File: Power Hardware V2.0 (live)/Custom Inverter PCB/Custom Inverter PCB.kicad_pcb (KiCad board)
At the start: 2 copper layers, 138 parts, among them J1 1714971, J2 1714971, J3 1714968, J4 SSQ-110-03-G-D, J5 SSQ-110-03-G-D, K1 1-1393210-3, K2 1-1393210-3, Q1 CSD19532Q5B, Q2 CSD19532Q5B, Q3 CSD19532Q5B, Q4 CSD19532Q5B, Q5 CSD19532Q5B, Q6 CSD19532Q5B, Q7 HCPL-181-06BE, Q8 HCPL-181-06BE, U1 DRV8300DIPWR, U2 NTR4170NT1G, U3 NTR4170NT1G, U4 TLV9004IPWR, U5 LAUNCHXL-F280049C

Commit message: footprint fixes
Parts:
- removed the C10 at (55.0, 116.9)
- removed the C10 at (104.0, 49.4)
- removed the C11 at (104.0, 52.5)
- removed the C11 at (119.0, 80.6)
- removed the C11 at (68.7, 108.3)
- removed the C12 at (108.5, 46.4)
- removed the C12 at (71.8, 108.3)
- removed the C12 at (119.0, 83.1)
- removed the C13 at (119.0, 85.6)
- removed the C13 at (108.5, 49.4)
- removed the C13 at (74.8, 108.3)
- removed the C14 at (119.0, 88.1)
- removed the C14 at (77.8, 108.3)
- removed the C14 at (108.5, 52.5)
- removed C16, C19: 0.01uF, Capacitor_SMD:C_0805_2012Metric
- removed C17, C18, C22, C25, C26, C27: 0.1uF, Capacitor_SMD:C_0805_2012Metric
- removed C20: 2.2uF, Capacitor_SMD:C_0805_2012Metric
- removed the C6 at (105.8, 121.0)
- removed the C6 at (99.6, 46.4)
- removed the C8 at (110.0, 121.0)
- removed the C8 at (99.6, 52.5)
- removed the C9 at (34.4, 116.9)
- removed the C9 at (104.0, 46.4)
- removed J4, J5: SSQ-110-03-G-D, SSQ_110_03_G_D (1):SAMTEC_SSQ-110-03-G-D
- removed K1: 1-1393210-3, T9AS1D12_12:TE_1-1393210-3
- removed Q7, Q8: HCPL-181-06BE, HCPL_181_06BE:HCPL-181_BRA
- removed the R10 at (68.7, 126.0)
- removed the R10 at (114.6, 80.8)
- removed the R10 at (103.9, 37.6)
- removed the R11 at (114.6, 83.8)
- removed the R11 at (71.7, 126.0)
- removed the R11 at (103.9, 40.5)
- removed the R12 at (74.6, 126.0)
- removed the R12 at (114.6, 86.7)
- removed the R12 at (103.9, 43.5)
- removed the R13 at (108.4, 28.7)
- removed the R13 at (119.0, 90.6)
- removed the R13 at (77.6, 126.0)
- removed the R14 at (108.4, 31.7)
- removed the R14 at (114.6, 89.7)
- removed the R14 at (80.5, 126.0)
- removed the R15 at (114.6, 92.6)
- removed the R15 at (108.4, 34.6)
- removed the R15 at (83.5, 126.0)
- removed the R16 at (83.4, 52.8)
- removed the R16 at (114.6, 95.5)
- removed the R17 at (83.4, 55.7)
- removed the R17 at (114.6, 98.5)
- removed R19, R21, R26, R27: 10K, Resistor_SMD:R_0805_2012Metric
- removed the R2 at (95.3, 126.0)
- removed the R2 at (99.5, 31.7)
- removed R20, R24, R25, R30, R31: 49.9K, Resistor_SMD:R_0805_2012Metric
- removed R22, R23, R28, R29: 4.99K, Resistor_SMD:R_0805_2012Metric
- removed the R3 at (98.3, 126.0)
- removed the R3 at (99.5, 34.6)
- removed R33, R37, R39, R41: 97.6K, Resistor_SMD:R_0805_2012Metric
- removed R34, R38, R40, R42: 3K, Resistor_SMD:R_0805_2012Metric
- removed the R4 at (99.5, 37.6)
- removed the R4 at (101.2, 126.0)
- removed the R5 at (99.5, 40.5)
- removed the R5 at (96.3, 119.5)
- removed the R6 at (104.2, 126.0)
- removed the R6 at (99.5, 43.5)
- removed the R7 at (107.1, 126.0)
- removed the R7 at (103.9, 28.7)
- removed the R9 at (103.9, 34.6)
- removed the R9 at (101.2, 119.5)
- removed VR1: UA78M33CDCYR, UA78M33CDCYR:VREG_UA78M33CDCYR
- added C10: 330 µF, EEV_FK2A331M:CAP_EEVFK2A331M, F.Cu at (155.7, 48.9)
- added C11: 220nF, Capacitor_SMD:C_0603_1608Metric, F.Cu at (162.6, 91.3)
- added C12: 220nF, Capacitor_SMD:C_0603_1608Metric, F.Cu at (162.6, 93.8)
- added C13: 220nF, Capacitor_SMD:C_0603_1608Metric, F.Cu at (162.6, 96.3)
- added C14: 220nF, Capacitor_SMD:C_0603_1608Metric, F.Cu at (162.6, 98.8)
- added C6: 1uF, Capacitor_SMD:C_1210_3225Metric, F.Cu at (134.7, 99.2)
- added C8: 1uF, Capacitor_SMD:C_1210_3225Metric, F.Cu at (134.7, 107.7)
- added C9: 330 µF, EEV_FK2A331M:CAP_EEVFK2A331M, F.Cu at (155.7, 28.3)
- added CR4: LD1085D2M33R, LD1085D2M33R:D2PAK&slash_A_STM, F.Cu at (150.5, 65.7)
- added F1: 250V 30A, 0463030_ER:FUSE_0463_LTF-M, F.Cu at (173.4, 68.6)
- added F2: 250V 30A, 0463030_ER:FUSE_0463_LTF-M, F.Cu at (142.7, 81.8)
- added F3: 250V 30A, 0463030_ER:FUSE_0463_LTF-M, F.Cu at (142.7, 86.7)
- added F4: 250V 30A, 0463030_ER:FUSE_0463_LTF-M, F.Cu at (142.7, 91.6)
- added J6: 1989764, PHOENIX_1989764:PHOENIX_1989764, F.Cu at (128.4, 133.4)
- added J7: 1714971, 1714971:PHOENIX_1714971, F.Cu at (124.6, 59.4)
- added J8: 1714971, 1714971:PHOENIX_1714971, F.Cu at (124.6, 73.5)
- added R10: 4.7K, Resistor_SMD:R_0805_2012Metric, F.Cu at (154.0, 91.5)
- added R11: 4.7K, Resistor_SMD:R_0805_2012Metric, F.Cu at (154.0, 94.4)
- added R12: 4.7K, Resistor_SMD:R_0805_2012Metric, F.Cu at (154.0, 97.4)
- added R13: 4.7K, Resistor_SMD:R_0805_2012Metric, F.Cu at (154.0, 100.3)
- added R14: 4.7K, Resistor_SMD:R_0805_2012Metric, F.Cu at (154.0, 103.3)
- added R15: 4.7K, Resistor_SMD:R_0805_2012Metric, F.Cu at (154.0, 106.2)
- added R16: 4.7K, Resistor_SMD:R_0805_2012Metric, F.Cu at (158.4, 91.5)
- added R17: 4.7K, Resistor_SMD:R_0805_2012Metric, F.Cu at (158.4, 94.4)
- added R2: 15R, Resistor_SMD:R_0805_2012Metric, F.Cu at (134.1, 83.8)
- added R3: 15R, Resistor_SMD:R_0805_2012Metric, F.Cu at (134.1, 86.7)
- added R4: 15R, Resistor_SMD:R_0805_2012Metric, F.Cu at (134.1, 89.7)
- added R45: 3K, Resistor_SMD:R_0805_2012Metric, F.Cu at (125.0, 133.9)
- added R46: 3K, Resistor_SMD:R_0805_2012Metric, F.Cu at (125.0, 136.9)
- added R47: 3K, Resistor_SMD:R_0805_2012Metric, F.Cu at (125.0, 139.8)
- added R48: 3K, Resistor_SMD:R_0805_2012Metric, F.Cu at (125.0, 142.8)
- added R5: 10k, Resistor_SMD:R_0805_2012Metric, F.Cu at (125.0, 122.1)
- added R6: 15R, Resistor_SMD:R_0805_2012Metric, F.Cu at (134.1, 92.6)
- added R7: 15R, Resistor_SMD:R_0805_2012Metric, F.Cu at (134.1, 95.6)
- added R9: 10k, Resistor_SMD:R_0805_2012Metric, F.Cu at (125.0, 128.0)
- added U6: OP292GSZ-REEL, OP292GSZ-REEL:R_8_ADI, F.Cu at (131.5, 137.5)
- J3: footprint 1714968:PHOENIX_1714968 -> PHOENIX_1714968:PHOENIX_1714968
- Q1, Q2, Q3, Q4, Q5, Q6: footprint CSD19532Q5B (1):TRANS_CSD19532Q5B -> CSD19532Q5B:TRANS_CSD19532Q5B
- R18: value 100k -> 10k
- R8: value 0.003R -> 10k; footprint Resistor_SMD:R_2512_6332Metric -> Resistor_SMD:R_0805_2012Metric
- TP1, TP2, TP3, TP4, TP5, TP6, TP7, TP8, TP9: footprint 5002 (1):KEYSTONE_5002 -> 5002:KEYSTONE_5002
- U2, U3: value NTR4170NT1G -> TLI4971A050T5E0001XUMA1; footprint NTR4170NT1G:SOT-23_ONS -> TLI4971A:PG-TISON-8-5
- U4: value TLV9004IPWR -> TLI4971A050T5E0001XUMA1; footprint TLV9004IPWR:SOP65P640X120-14N -> TLI4971A:PG-TISON-8-5
- moved R43 146.9 mm to (169.2, 72.5), turned to 0 degrees
- moved J3 145.4 mm to (168.8, 65.4)
- moved R44 143.4 mm to (169.2, 75.4), turned to 0 degrees
- moved C28 130.2 mm to (158.8, 75.7), turned to 0 degrees
- moved U5 126.8 mm to (84.8, 75.4), turned to 0 degrees
- moved U3 119.3 mm to (167.7, 84.7)
- moved K2 115.1 mm to (175.8, 44.2)
- moved CR2 114.8 mm to (191.8, 70.6)
- moved CR1 114.8 mm to (191.8, 67.6)
- moved CR3 114.8 mm to (191.8, 73.7)
- moved U2 109.0 mm to (157.0, 84.7)
- moved U1 108.1 mm to (184.6, 70.3)
- moved C23 98.2 mm to (166.8, 94.5), turned to 0 degrees
- moved R8 95.8 mm to (125.0, 125.1)
- moved C24 95.1 mm to (166.8, 97.5), turned to 0 degrees
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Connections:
- C1 pad 1: +3.3VDC -> +3.3V
- C15 pad 1: /Current sense/SBLO -> +5V
- R18 pad 1: +3.3V -> +5V
- R18 pad 2: /Current sense/4- -> Net-(U6--INB)
- R8 pad 1: /Half_Bridges/SBHI -> +5V
- R8 pad 2: +100VDC -> Net-(U6--INA)
- U2 pad 1: Net-(U2-GATE) -> +3.3V
- U2 pad 2: +100VDC -> GND
- U2 pad 3: Net-(U2-DRAIN) -> /Current sense/Vref
- U3 pad 1: Net-(U3-GATE) -> +3.3V
- U3 pad 2: +100VDC -> GND
- U3 pad 3: Net-(U3-DRAIN) -> /Current sense/Vref
- U4 pad 1: /Current sense/1_Out -> +3.3V
- U4 pad 2: /Current sense/1- -> GND
- U4 pad 3: /Current sense/1+ -> /Current sense/Vref
- U4 pad 4: +3.3V -> /Current sense/3_Out
- U4 pad 5: /Current sense/2+ -> /Current sense/OCD1_C
- U4 pad 6: /Current sense/2- -> /Current sense/OCD2_C
- U4 pad 7: /Current sense/2_Out -> /Current sense/IB-
- U4 pad 8: /Current sense/3_Out -> /SHB
- U5 pad J7_63: unconnected-(U5A-ADCINA6-PadJ7_63) -> /MCU/SINE
- U5 pad J7_64: unconnected-(U5A-ADCINA2-PadJ7_64) -> /MCU/COS
- U5 pad J7_65: unconnected-(U5A-ADCINC14-PadJ7_65) -> /Current sense/Vref
- U5 pad J7_66: unconnected-(U5A-ADCINC1-PadJ7_66) -> /SEN_100V
- U5 pad J7_67: unconnected-(U5A-ADCINC3_P4I-PadJ7_67) -> /Current sense/ISENA
- U5 pad J7_68: unconnected-(U5A-ADCINC5_P6I-PadJ7_68) -> /Current sense/ISENB
- U5 pad J7_69: unconnected-(U5A-ADCINA3_P21-PadJ7_69) -> /Current sense/ISENC
- U5 pad J8_75: unconnected-(U5A-GPIO3-PadJ8_75) -> /INLC
- U5 pad J8_76: unconnected-(U5A-GPIO2_BP-PadJ8_76) -> /INHC
- U5 pad J8_77: unconnected-(U5A-GPIO7_BP-PadJ8_77) -> /INLC
- U5 pad J8_78: unconnected-(U5A-GPIO6_BP-PadJ8_78) -> /INHB
- U5 pad J8_79: unconnected-(U5A-GPIO1-PadJ8_79) -> /INLA
- U5 pad J8_80: unconnected-(U5A-GPIO0-PadJ8_80) -> /INHA

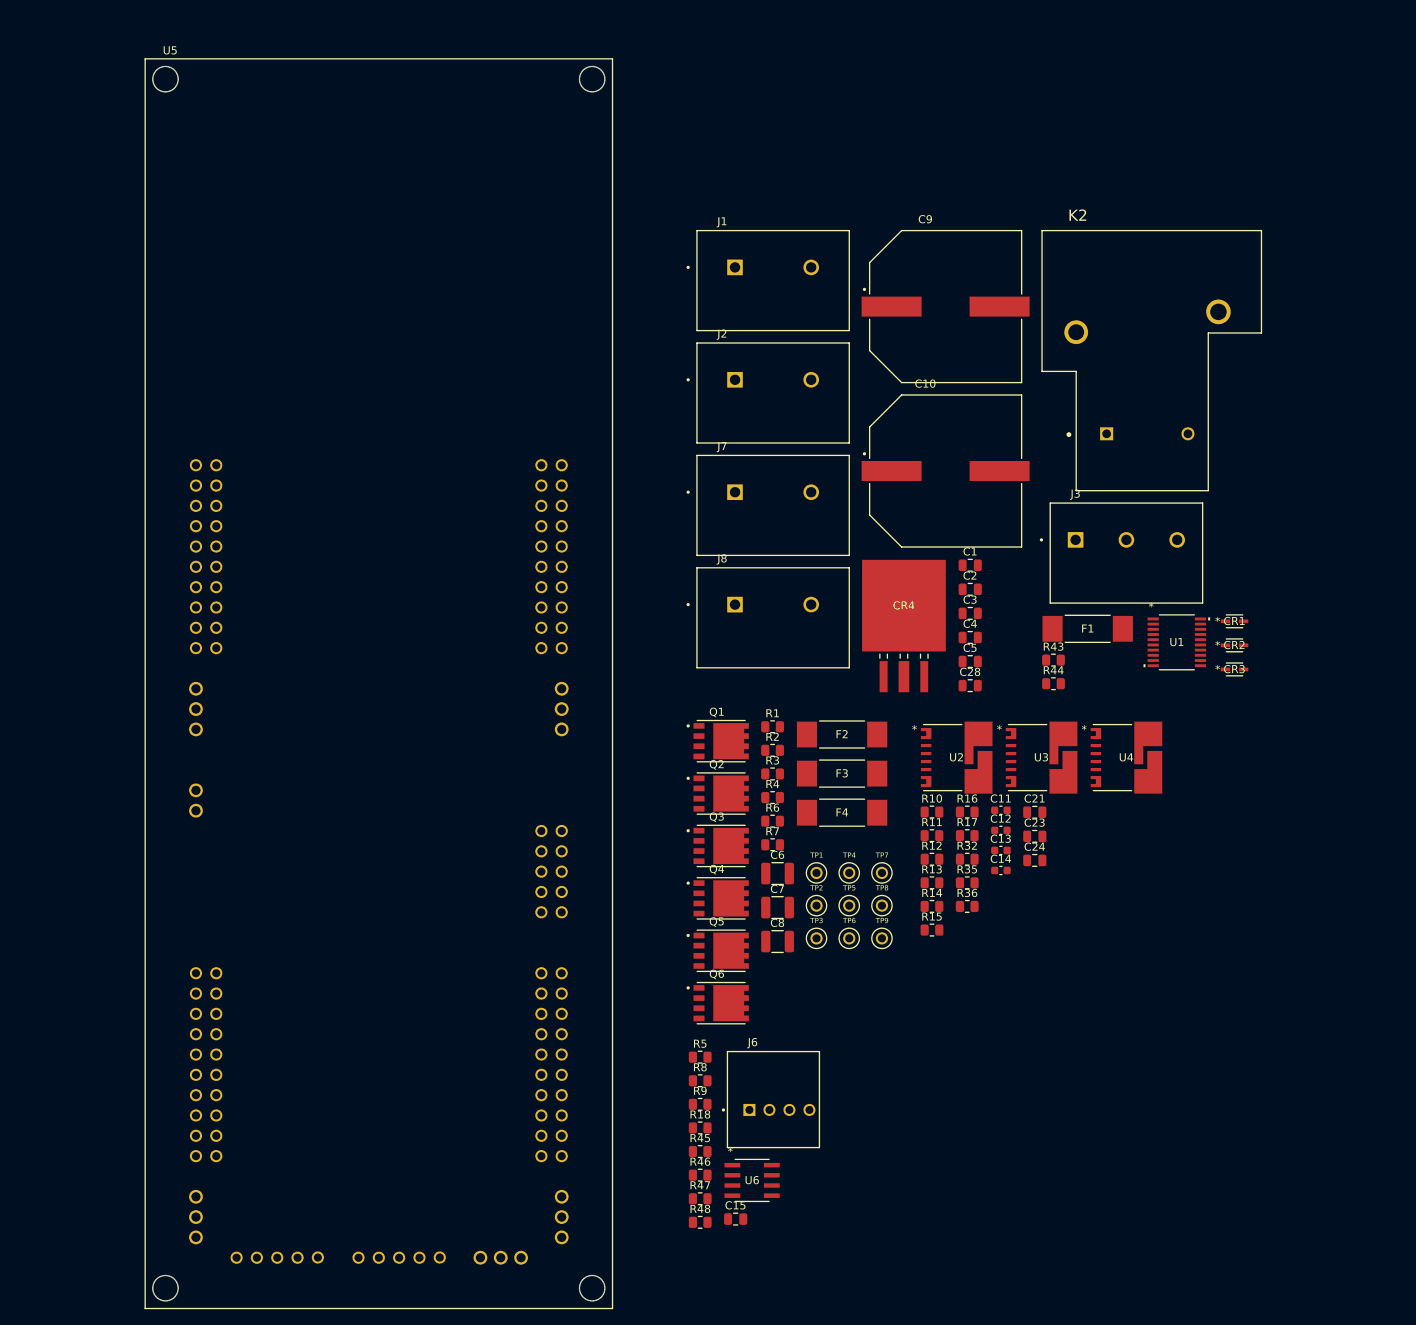
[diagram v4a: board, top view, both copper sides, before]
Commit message: Pcb layout and tracing
changed footprint file for current sense ic
did layout and tracing for pcb
created bom
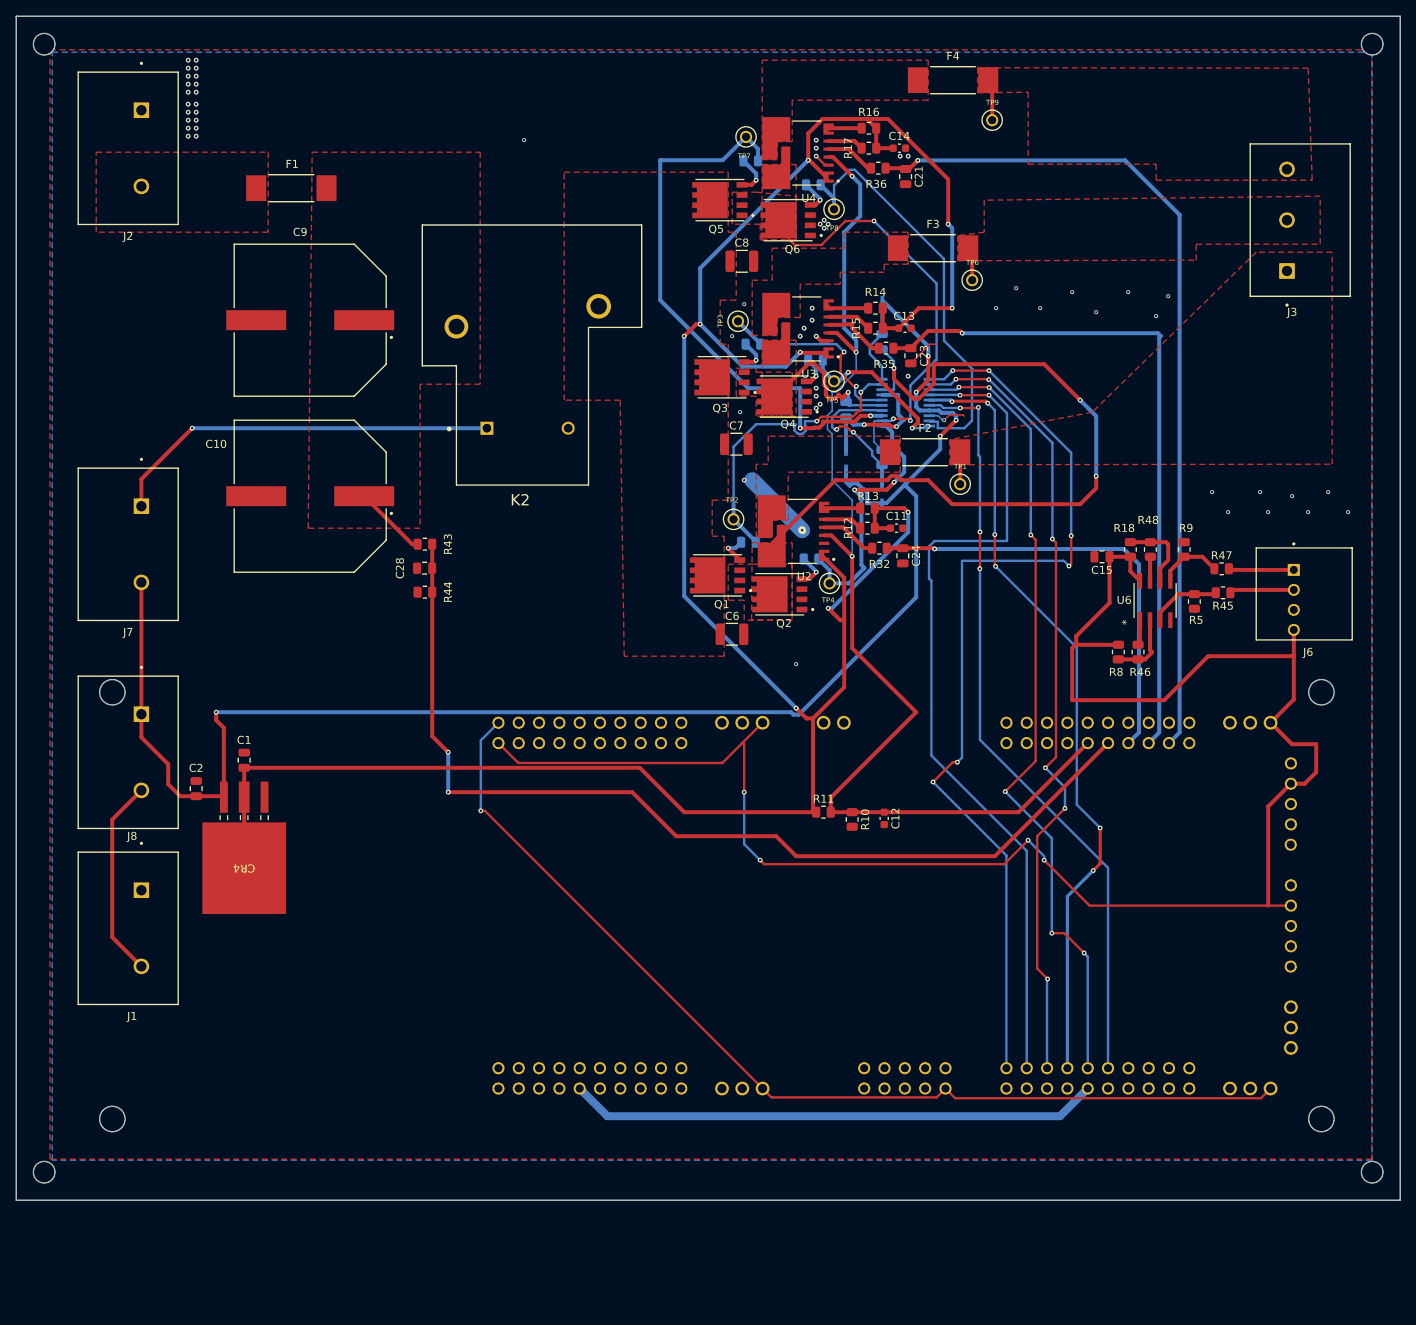
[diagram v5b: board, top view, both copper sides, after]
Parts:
- added REF**: MountingHole_2.7mm_M2.5, MountingHole:MountingHole_2.7mm_M2.5, F.Cu at (43.0, -4.50)
- added REF**: MountingHole_2.7mm_M2.5, MountingHole:MountingHole_2.7mm_M2.5, F.Cu at (209.0, -4.50)
- added REF**: MountingHole_2.7mm_M2.5, MountingHole:MountingHole_2.7mm_M2.5, F.Cu at (43.0, 136.5)
- added REF**: MountingHole_2.7mm_M2.5, MountingHole:MountingHole_2.7mm_M2.5, F.Cu at (209.0, 136.5)
- C3, C4, C5, CR1, CR2, CR3, R1, R2, R3, R4, R6, R7, U1, U5: moved to B.Cu
- U2, U3, U4: footprint TLI4971A:PG-TISON-8-5 -> TLI4971A:IC_TLI4971A050T5UE0001XUMA1
- moved F1 113.8 mm to (73.9, 13.5)
- moved TP9 103.2 mm to (161.5, 5.00)
- moved R47 102.2 mm to (190.2, 61.1)
- moved R48 101.2 mm to (181.3, 58.7), turned to 90 degrees
- moved J1 101.2 mm to (47.2, 96.5), turned to -90 degrees
- moved J6 99.9 mm to (194.5, 58.5), turned to -90 degrees
- moved C2 99.9 mm to (62.0, 88.5), turned to 90 degrees
- moved Q6 98.2 mm to (136.0, 17.5), turned to 180 degrees
- moved R45 95.7 mm to (190.4, 64.1), turned to 180 degrees
- moved C15 94.6 mm to (175.2, 59.6), turned to 180 degrees
- moved C1 94.0 mm to (68.0, 85.0), turned to 90 degrees
- moved Q5 93.8 mm to (127.5, 15.0), turned to 180 degrees
- moved TP7 93.6 mm to (130.7, 7.08), turned to 90 degrees
- moved R36 92.9 mm to (147.3, 11.0)
- moved F4 92.6 mm to (156.6, 0.00)
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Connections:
- C1 pad 1: +3.3V -> +3.3VDC
- C11 pad 2: +3.3V -> +3.3VDC
- C13 pad 2: +3.3V -> +3.3VDC
- C14 pad 2: +3.3V -> +3.3VDC
- CR4 pad 2: +3.3V -> +3.3VDC
- CR4 pad 4: +3.3V -> +3.3VDC
- Q1 pad 2: (no net) -> /SHA
- Q1 pad 3: (no net) -> /SHA
- Q2 pad 2: (no net) -> GND
- Q2 pad 3: (no net) -> GND
- Q3 pad 2: (no net) -> /SHB
- Q3 pad 3: (no net) -> /SHB
- Q4 pad 2: (no net) -> GND
- Q4 pad 3: (no net) -> GND
- Q5 pad 2: (no net) -> /SHC
- Q5 pad 3: (no net) -> /SHC
- Q6 pad 2: (no net) -> GND
- Q6 pad 3: (no net) -> GND
- R11 pad 1: +3.3V -> +3.3VDC
- R12 pad 1: +3.3V -> +3.3VDC
- R13 pad 1: +3.3V -> +3.3VDC
- R14 pad 1: +3.3V -> +3.3VDC
- R15 pad 1: +3.3V -> +3.3VDC
- R16 pad 1: +3.3V -> +3.3VDC
- R17 pad 1: +3.3V -> +3.3VDC
- U1 pad 5: /INLC -> /INLB
- U2 pad 1: +3.3V -> +3.3VDC
- U3 pad 1: +3.3V -> +3.3VDC
- U4 pad 1: +3.3V -> +3.3VDC
- U4 pad 7: /Current sense/IB- -> /Current sense/IC-
- U4 pad 8: /SHB -> /SHC
- U5 pad J8_77: /INLC -> /INLB
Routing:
- net +3.3VDC: track 0.00 -> 314.3 mm, vias 0 -> 9
- net +5V: track 0.00 -> 227.7 mm, vias 0 -> 4
- net +12VDC: track 0.00 -> 198.7 mm, vias 0 -> 5
- net /Current sense/Vref: track 0.00 -> 141.1 mm, vias 0 -> 3
- net +3.3V: track 0.00 -> 127.0 mm, vias 0 -> 1
- net /SEN_100V: track 0.00 -> 123.5 mm, vias 0 -> 2
- net /INHA: track 0.00 -> 119.4 mm, vias 0 -> 6
- net /INLA: track 0.00 -> 106.9 mm, vias 0 -> 2
- net /Current sense/ISENC: track 0.00 -> 106.6 mm, vias 0 -> 1
- net /INHC: track 0.00 -> 101.9 mm, vias 0 -> 6
- net /INHB: track 0.00 -> 100.9 mm, vias 0 -> 6
- net /SHA: track 0.00 -> 98.7 mm, vias 0 -> 3
- net /INLB: track 0.00 -> 98.2 mm, vias 0 -> 6
- net /INLC: track 0.00 -> 95.6 mm, vias 0 -> 4
- net /Current sense/ISENB: track 0.00 -> 86.1 mm, vias 0 -> 1
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- added copper zone on F.Cu, net +100VDC
- added copper zone on F.Cu, net +100VDC to Relay
- added copper zone on F.Cu, net /Current sense/IA-
- added copper zone on F.Cu, net /Current sense/IB-
- added copper zone on F.Cu, net /Current sense/IC-
- added copper zone on F.Cu, net /MOTA
- added copper zone on F.Cu, net /MOTB
- added copper zone on F.Cu, net /MOTC
- added copper zone on F.Cu, net /SHA
- added copper zone on F.Cu, net /SHB
- added copper zone on F.Cu, net /SHC
- added copper zone on B.Cu, net GND
- added copper zone on F.Cu, net GND
- added copper zone on F.Cu, net Net-(F1-Pad1)
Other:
- board outline added: 173 x 148 mm

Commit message: PCB Fixes
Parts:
- removed REF** (x4): MountingHole_2.7mm_M2.5, MountingHole:MountingHole_2.7mm_M2.5
- moved J2 60.5 mm to (103.5, 21.1), turned to 180 degrees
- moved C2 56.8 mm to (72.6, 144.3), turned to -90 degrees
- moved C1 53.7 mm to (68.4, 138.7), turned to 180 degrees
- moved J7 48.4 mm to (81.8, 82.4), turned to 0 degrees
- moved J1 45.3 mm to (42.0, 51.5)
- moved CR4 42.4 mm to (81.6, 138.7), turned to -90 degrees
- moved R11 32.2 mm to (166.6, 110.2), turned to 180 degrees
- moved R43 28.2 mm to (77.2, 82.8)
- moved C28 27.8 mm to (77.1, 85.4)
- moved R44 27.4 mm to (77.2, 87.9)
- moved R10 26.8 mm to (163.4, 110.8)
- moved C11 26.5 mm to (137.8, 79.8)
- moved C14 26.5 mm to (138.2, 32.3)
- moved R16 26.5 mm to (134.4, 29.8)
- moved R17 26.5 mm to (134.4, 32.3)
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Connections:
- net Net-(F1-Pad1) renamed /GateDriver&Power Inputs/PVDD
- C1 pad 1: +3.3VDC -> +3.3V
- C11 pad 2: +3.3VDC -> +3.3V
- C13 pad 2: +3.3VDC -> +3.3V
- C14 pad 2: +3.3VDC -> +3.3V
- CR4 pad 2: +3.3VDC -> +3.3V
- CR4 pad 4: +3.3VDC -> +3.3V
- R11 pad 1: +3.3VDC -> +3.3V
- R12 pad 1: +3.3VDC -> +3.3V
- R13 pad 1: +3.3VDC -> +3.3V
- R14 pad 1: +3.3VDC -> +3.3V
- R15 pad 1: +3.3VDC -> +3.3V
- R16 pad 1: +3.3VDC -> +3.3V
- R17 pad 1: +3.3VDC -> +3.3V
- U2 pad 1: +3.3VDC -> +3.3V
- U3 pad 1: +3.3VDC -> +3.3V
- U4 pad 1: +3.3VDC -> +3.3V
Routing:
- net +3.3V: track 127.0 -> 463.0 mm, vias 1 -> 7
- net +3.3VDC: track 314.3 -> 0.00 mm, vias 9 -> 0
- net /SHA: track 98.7 -> 45.8 mm, vias 3 -> 1
- net Net-(J7-Pad1): track 49.2 -> 0.00 mm, vias 1 -> 0
- net GND: track 22.3 -> 57.4 mm, vias 63 -> 740
- net +5V: track 227.7 -> 192.9 mm, vias 4 -> 0
- net +12V to relay: track 25.0 -> 0.00 mm
- net /Current sense/Vref: track 141.1 -> 116.1 mm, vias 3 -> 4
- net /Current sense/ISENB: track 86.1 -> 101.2 mm, vias 1 -> 2
- net /Current sense/ISENA: track 55.3 -> 70.0 mm
- net /INLC: track 95.6 -> 108.9 mm, vias 4 -> 2
- net +12VDC: track 198.7 -> 211.0 mm, vias 5 -> 46
- net /Current sense/ISENC: track 106.6 -> 117.2 mm, vias 1 -> 2
- net /SEN_100V: track 123.5 -> 114.2 mm, vias 2 -> 3
- net /INLB: track 98.2 -> 107.1 mm, vias 6 -> 2
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- added copper zone on B.Cu, net +100VDC to Relay
- added copper zone on F.Cu, net +12V to relay
- added copper zone on B.Cu, net +12VDC
- added copper zone on F.Cu, net +12VDC
- added copper zone on B.Cu, net /Current sense/IB-
- added copper zone on B.Cu, net /Current sense/IC-
- added copper zone on B.Cu, net /GateDriver&Power Inputs/PVDD
- added copper zone on B.Cu, net /MOTA
- added copper zone on B.Cu, net /MOTB
- added copper zone on B.Cu, net /MOTC
- added copper zone on B.Cu, net Net-(J7-Pad1)
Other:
- board size 173 x 148 mm -> 166 x 143 mm
- board text added: "12V"
- board text added: "12V CNTRL"
- board text added: "GND"
- board text added: "INVERTER HARDWARE V2.0 M.Nguyen C.O'Brien D.Posala A.Truong"
- board text added: "RELAY CNTRL"
